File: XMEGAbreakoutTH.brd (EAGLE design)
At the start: 160 x 100 mm, 22 parts, among them IC1 XMEGA16A4

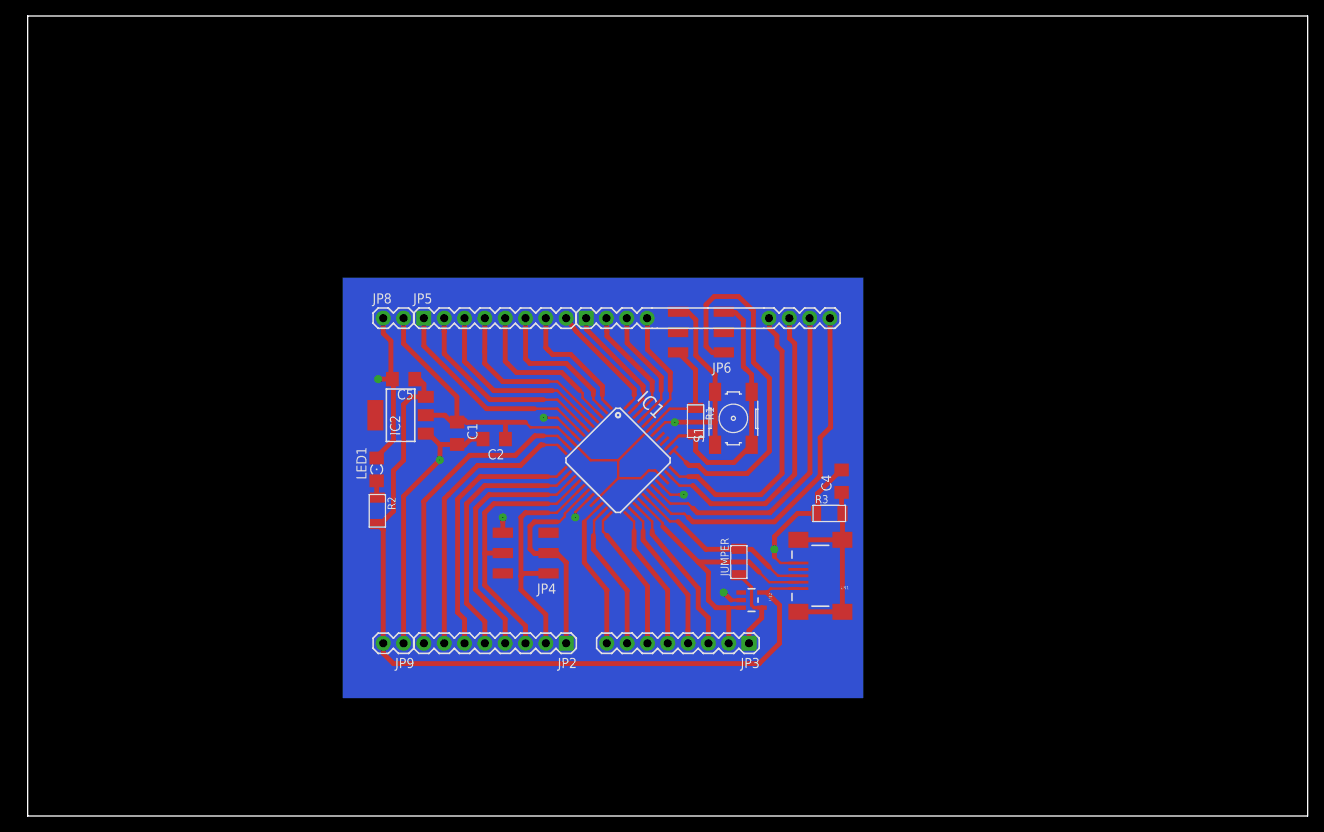
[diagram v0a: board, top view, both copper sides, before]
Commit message: change th dim
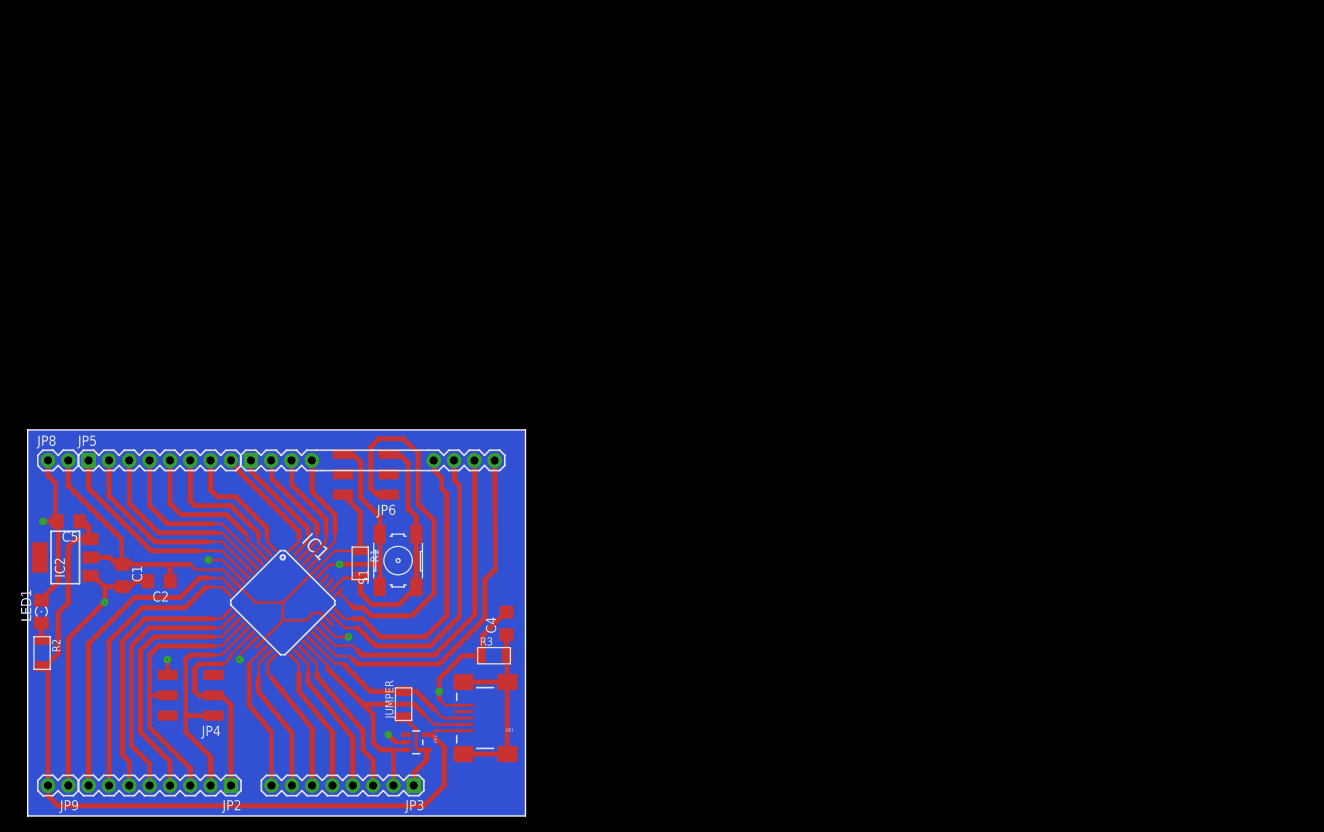
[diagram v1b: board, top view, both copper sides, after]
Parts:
- moved C4 45.5 mm to (59.8, 24.1)
- moved C5 45.5 mm to (5.08, 36.8)
- moved IC2 45.5 mm to (4.70, 32.3)
- moved JP2 45.5 mm to (25.4, 3.81)
- moved JP3 45.5 mm to (48.3, 3.81)
- moved JP4 45.5 mm to (20.3, 15.1)
- moved JP9 45.5 mm to (5.08, 3.81)
- moved JUMPER 45.5 mm to (47.0, 14.0)
- moved LED1 45.5 mm to (1.71, 25.5)
- moved R1 45.5 mm to (41.6, 31.6)
- moved R2 45.5 mm to (1.80, 20.4)
- moved S1 45.5 mm to (46.3, 31.9)
- moved C1 45.5 mm to (11.8, 30.1)
- moved C2 45.5 mm to (16.4, 29.3)
- moved IC1 45.5 mm to (31.9, 26.7)
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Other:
- board size 160 x 100 mm -> 62.2 x 48.3 mm

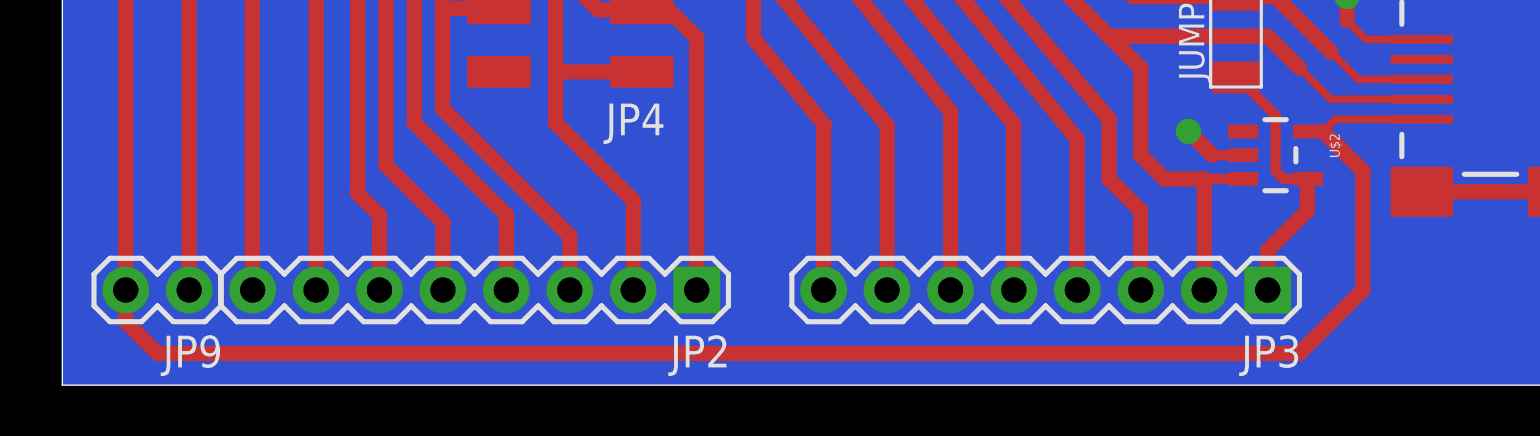
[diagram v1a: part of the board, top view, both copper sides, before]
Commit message: solder jumper on 5V
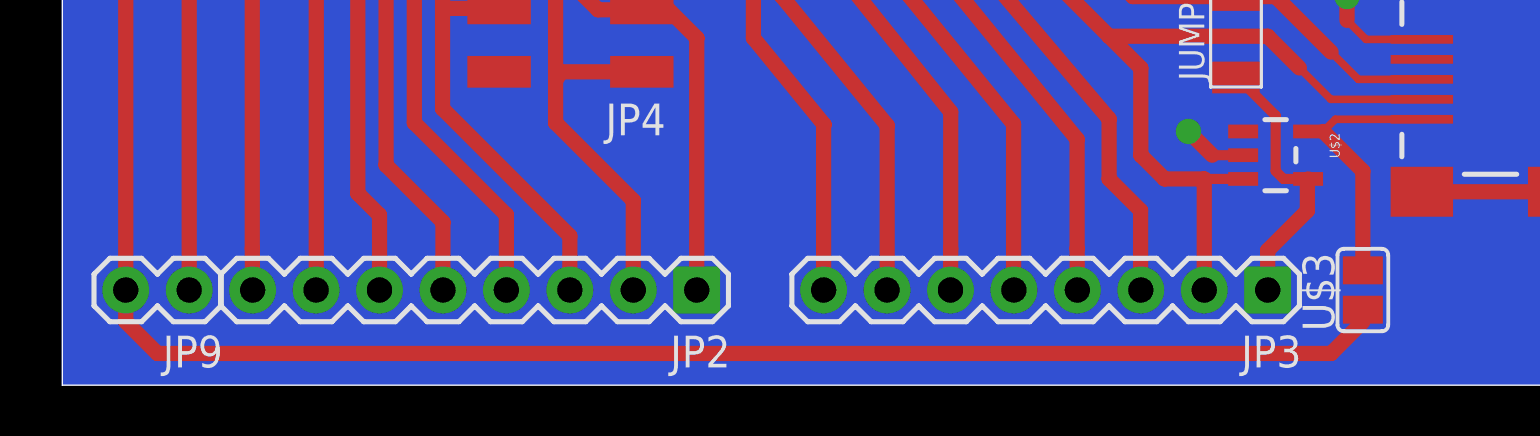
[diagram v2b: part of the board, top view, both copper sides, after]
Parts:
- added U$3: SOLDER_JUMPER, fab:SJFAB
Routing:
- net VBUS: track 102.2 -> 100.4 mm
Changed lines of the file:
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@@
 <layer number="14" name="Route14" color="1" fill="6" visible="no" active="no"/>
 <layer number="15" name="Route15" color="4" fill="6" visible="no" active="no"/>
-<layer number="16" name="Bottom" color="1" fill="1" visible="no" active="yes"/>
+<layer number="16" name="Bottom" color="1" fill="1" visible="yes" active="yes"/>
 <layer number="17" name="Pads" color="2" fill="1" visible="yes" active="yes"/>
 <layer number="18" name="Vias" color="2" fill="1" visible="yes" active="yes"/>
@@
 <element name="JP6" library="fab" package="2X03SMD" value="" x="42.251265625" y="42.712053125" rot="R180"/>
 <element name="JUMPER" library="fab" package="R1206FAB" value="0Ohm" x="46.99" y="13.97" rot="R90"/>
+<element name="U$3" library="fab" package="SJFAB" value="SOLDER_JUMPER" x="52.07" y="3.81" rot="R90"/>
 </elements>
 <signals>
@@
 <wire x1="2.54" y1="3.81" x2="2.54" y2="2.54" width="0.6096" layer="1"/>
 <wire x1="2.54" y1="2.54" x2="3.81" y2="1.27" width="0.6096" layer="1"/>
-<wire x1="3.81" y1="1.27" x2="49.53" y2="1.27" width="0.6096" layer="1"/>
-<wire x1="49.53" y1="1.27" x2="52.07" y2="3.81" width="0.6096" layer="1"/>
-<wire x1="52.07" y1="3.81" x2="52.07" y2="8.5725" width="0.6096" layer="1"/>
+<wire x1="3.81" y1="1.27" x2="50.8" y2="1.27" width="0.6096" layer="1"/>
+<wire x1="52.07" y1="8.5725" x2="52.07" y2="5.08" width="0.6096" layer="1"/>
+<wire x1="50.8" y1="1.27" x2="52.07" y2="2.54" width="0.6096" layer="1"/>
+<wire x1="52.07" y1="2.54" x2="52.07" y2="5.08" width="0" layer="19" extent="1-1"/>
 </signal>
 <signal name="D+">

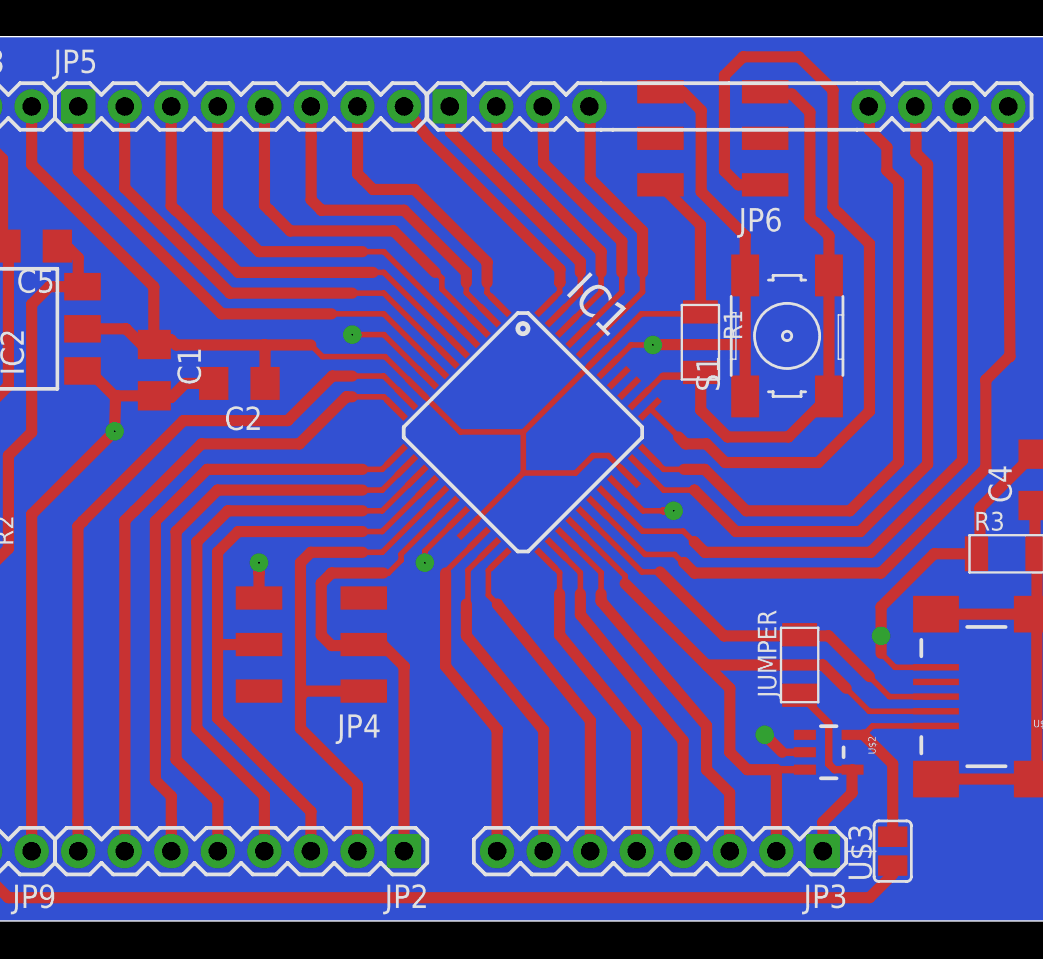
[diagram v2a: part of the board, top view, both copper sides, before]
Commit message: caps on each port
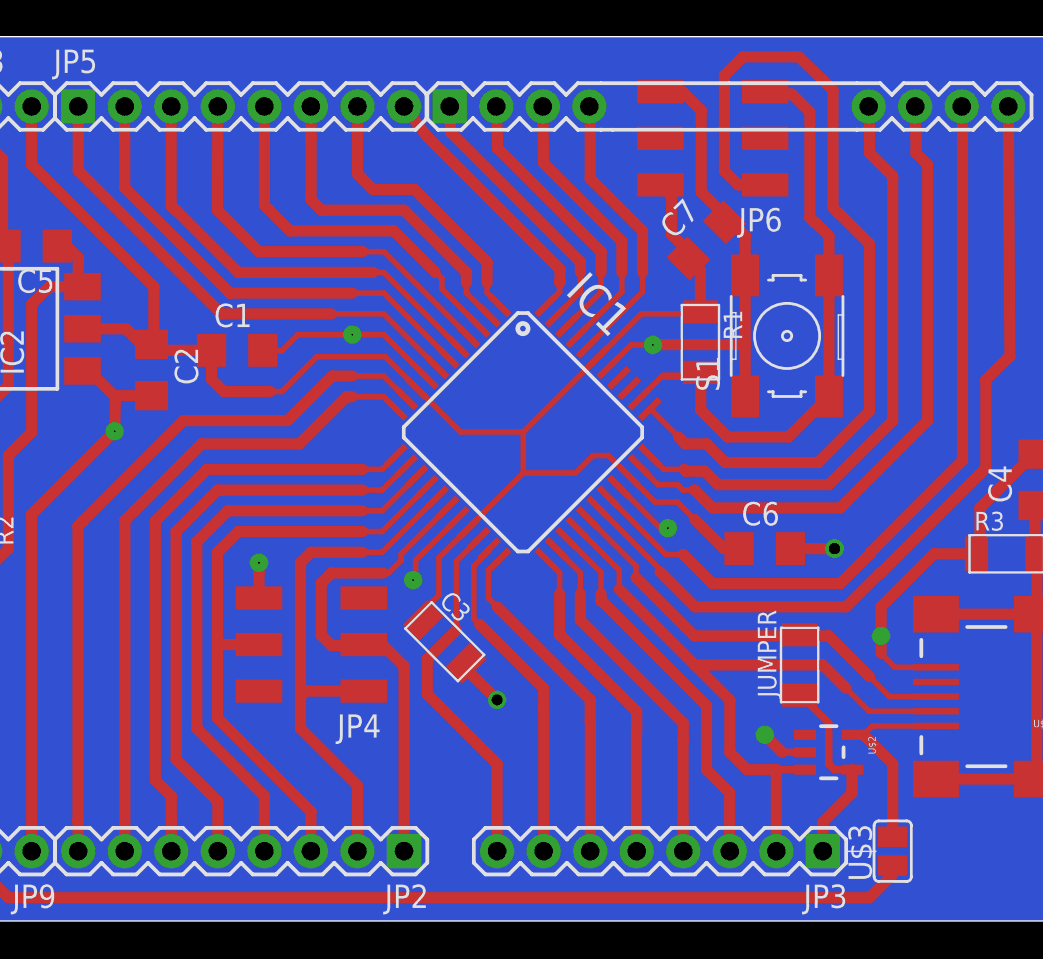
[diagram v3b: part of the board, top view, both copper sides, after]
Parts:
- added C3: 0.1uF, fab:C1206FAB
- added C6, C7: 0.1uF, fab:C1206
- moved C2 4.85 mm to (11.6, 30.1), turned to 270 degrees
- moved C1 4.65 mm to (16.3, 31.1), turned to 0 degrees
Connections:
- net GND: now also C3.2, C6.2, C7.2
- net VCC: now also C3.1, C6.1, C7.1
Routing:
- net GND: track 225.4 -> 239.0 mm, vias 9 -> 11
- net VCC: track 79.5 -> 92.2 mm
- net PE3: track 36.0 -> 33.0 mm
- net PE2: track 38.5 -> 36.1 mm
- net PE0: track 45.3 -> 46.9 mm
- net PE1: track 42.0 -> 43.4 mm
- net N$24: track 18.8 -> 19.8 mm
- net D-: track 38.2 -> 38.8 mm
- net N$23: track 19.0 -> 18.4 mm

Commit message: 600dpi
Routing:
- net GND: track 239.0 -> 259.3 mm, vias 11 -> 14
